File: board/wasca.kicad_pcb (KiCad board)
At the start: 2 copper layers, 0 parts

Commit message: PCB routing started
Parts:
- added C1: 10uF, Capacitors_SMD:C_0603_HandSoldering, F.Cu at (118.5, 90.9)
- added C10: 0.1uF, Capacitors_SMD:C_0603_HandSoldering, F.Cu at (123.1, 117.7)
- added C11: 0.1uF, Capacitors_SMD:C_0603_HandSoldering, F.Cu at (98.6, 121.4)
- added C12: 0.1uF, Capacitors_SMD:C_0603_HandSoldering, F.Cu at (90.4, 114.0)
- added C13: 0.1uF, Capacitors_SMD:C_0603_HandSoldering, F.Cu at (126.5, 109.2)
- added C14: 0.1uF, Capacitors_SMD:C_0603_HandSoldering, F.Cu at (153.3, 128.8)
- added C15: 0.1uF, Capacitors_SMD:C_0603_HandSoldering, F.Cu at (130.6, 123.8)
- added C16: 0.1uF, Capacitors_SMD:C_0603_HandSoldering, F.Cu at (103.0, 113.4)
- added C17: 0.1uF, Capacitors_SMD:C_0603_HandSoldering, F.Cu at (106.3, 126.7)
- added C18: 0.1uF, Capacitors_SMD:C_0603_HandSoldering, F.Cu at (159.4, 99.1)
- added C19: 0.1uF, Capacitors_SMD:C_0603_HandSoldering, F.Cu at (146.6, 96.0)
- added C2: 0.1uF, Capacitors_SMD:C_0603_HandSoldering, F.Cu at (78.1, 116.5)
- added C20: 0.1uF, Capacitors_SMD:C_0603_HandSoldering, F.Cu at (140.8, 113.0)
- added C21: 0.1uF, Capacitors_SMD:C_0603_HandSoldering, F.Cu at (113.9, 121.9)
- added C22: 0.1uF, Capacitors_SMD:C_0603_HandSoldering, F.Cu at (91.6, 126.1)
- added C23: 0.1uF, Capacitors_SMD:C_0603_HandSoldering, F.Cu at (96.1, 114.2)
- added C24: 0.1uF, Capacitors_SMD:C_0603_HandSoldering, F.Cu at (158.9, 117.6)
- added C25: 10uF, Capacitors_SMD:C_1206_HandSoldering, F.Cu at (149.7, 117.6)
- added C26: 0.1uF, Capacitors_SMD:C_0603_HandSoldering, F.Cu at (169.2, 116.2)
- added C27: 0.1uF, Capacitors_SMD:C_0603_HandSoldering, F.Cu at (155.7, 104.6)
- added C28: 0.1uF, Capacitors_SMD:C_0603_HandSoldering, F.Cu at (103.6, 64.6)
- added C29: 0.1uF, Capacitors_SMD:C_0603_HandSoldering, F.Cu at (93.6, 71.6)
- added C3: 0.1uF, Capacitors_SMD:C_0603_HandSoldering, F.Cu at (134.2, 116.0)
- added C30: 0.1uF, Capacitors_SMD:C_0603_HandSoldering, F.Cu at (80.8, 96.3)
- added C31: 0.1uF, Capacitors_SMD:C_0603_HandSoldering, F.Cu at (79.6, 104.9)
- added C32: 0.1uF, Capacitors_SMD:C_0603_HandSoldering, F.Cu at (106.8, 102.2)
- added C33: 10uF, Capacitors_SMD:C_1206_HandSoldering, F.Cu at (116.3, 100.1)
- added C34: 0.1uF, Capacitors_SMD:C_0603_HandSoldering, F.Cu at (125.1, 91.6)
- added C35: 0.1uF, Capacitors_SMD:C_0603_HandSoldering, F.Cu at (140.0, 100.2)
- added C36: 0.1uF, Capacitors_SMD:C_0603_HandSoldering, F.Cu at (83.2, 124.5)
- added C37: 0.1uF, Capacitors_SMD:C_0603_HandSoldering, F.Cu at (112.6, 62.0)
- added C38: 0.1uF, Capacitors_SMD:C_0603_HandSoldering, F.Cu at (97.9, 127.0)
- added C39: 0.1uF, Capacitors_SMD:C_0603_HandSoldering, F.Cu at (140.7, 120.9)
- added C4: 0.1uF, Capacitors_SMD:C_0603_HandSoldering, F.Cu at (106.9, 92.5)
- added C40: 0.1uF, Capacitors_SMD:C_0603_HandSoldering, F.Cu at (88.9, 86.7)
- added C41: 0.1uF, Capacitors_SMD:C_0603_HandSoldering, F.Cu at (89.8, 79.4)
- added C42: 0.1uF, Capacitors_SMD:C_0603_HandSoldering, F.Cu at (128.4, 130.8)
- added C43: 1uF, Capacitors_SMD:C_0603_HandSoldering, F.Cu at (128.1, 100.7)
- added C44: 0.1uF, Capacitors_SMD:C_0603_HandSoldering, F.Cu at (184.4, 61.1)
- added C45: 0.1uF, Capacitors_SMD:C_0603_HandSoldering, F.Cu at (91.6, 63.6)
- added C46: 0.1uF, Capacitors_SMD:C_0603_HandSoldering, F.Cu at (126.0, 53.5)
- added C47: 0.1uF, Capacitors_SMD:C_0603_HandSoldering, F.Cu at (85.1, 73.2)
- added C48: 0.1uF, Capacitors_SMD:C_0603_HandSoldering, F.Cu at (76.1, 89.4)
- added C49: 0.1uF, Capacitors_SMD:C_0603_HandSoldering, F.Cu at (101.0, 59.1)
- added C5: 0.1uF, Capacitors_SMD:C_0603_HandSoldering, F.Cu at (168.0, 130.7)
- added C50: 0.1uF, Capacitors_SMD:C_0603_HandSoldering, F.Cu at (97.5, 89.4)
- added C6: 0.1uF, Capacitors_SMD:C_0603_HandSoldering, F.Cu at (120.3, 125.3)
- added C7: 0.1uF, Capacitors_SMD:C_0603_HandSoldering, F.Cu at (110.0, 118.0)
- added C8: 0.1uF, Capacitors_SMD:C_0603_HandSoldering, F.Cu at (161.8, 109.0)
- added C9: 0.1uF, Capacitors_SMD:C_0603_HandSoldering, F.Cu at (139.8, 127.5)
- added CN1: CARTRIDGE_EDGE_CONNECTOR, Wasca:CARTRIDGE_EDGE_CONNECTOR2, F.Cu at (91.6, 152.3)
- added CON1: SD_Card, Connect:SD_Card_Receptacle, F.Cu at (205.3, 96.1)
- added CON2: USB_OTG, Connect:USB_Micro-B, F.Cu at (76.1, 59.3)
- added D1: D_Schottky_x2_KCom_AAK, Housings_SOT-23_SOT-143_TSOT-6:SOT-23_Handsoldering, F.Cu at (121.2, 61.3)
- added IC1: MT48LC32M16A2TG, Wasca:TSOP_II_54, F.Cu at (133.1, 49.5)
- added L1: L_Small, Resistors_SMD:R_0603_HandSoldering, F.Cu at (83.2, 81.4)
- added R1: 50K, Resistors_SMD:R_0603_HandSoldering, F.Cu at (132.6, 95.6)
- added R2: 50K, Resistors_SMD:R_0603_HandSoldering, F.Cu at (162.4, 58.3)
- added R3: 50K, Resistors_SMD:R_0603_HandSoldering, F.Cu at (147.1, 85.7)
- added R4: 50K, Resistors_SMD:R_0603_HandSoldering, F.Cu at (135.3, 105.5)
- added R5: 50K, Resistors_SMD:R_0603_HandSoldering, F.Cu at (211.3, 75.4)
- added R6: 27, Resistors_SMD:R_0603_HandSoldering, F.Cu at (199.6, 68.8)
- added R7: 27, Resistors_SMD:R_0603_HandSoldering, F.Cu at (191.4, 71.0)
- added R8: 4.7K, Resistors_SMD:R_0603_HandSoldering, F.Cu at (169.8, 109.0)
- added R9: 4.7K, Resistors_SMD:R_0603_HandSoldering, F.Cu at (162.9, 124.0)
- added U1: 74ALVC164245, Housings_SSOP:TSSOP-48_6.1x12.5mm_Pitch0.5mm, F.Cu at (94.5, 100.2)
- added U2: 74ALVC164245, Housings_SSOP:TSSOP-48_6.1x12.5mm_Pitch0.5mm, F.Cu at (134.0, 78.5)
- added U3: 74ALVC164245, Housings_SSOP:TSSOP-48_6.1x12.5mm_Pitch0.5mm, F.Cu at (120.0, 76.9)
- added U4: 74ALVC164245, Housings_SSOP:TSSOP-48_6.1x12.5mm_Pitch0.5mm, F.Cu at (103.6, 78.0)
- added U5: LD1117S33CTR, SMD_Packages:SOT-223, F.Cu at (178.6, 126.4)
- added U6: 10M04SFE144C8G, Housings_QFP:TQFP-144_20x20mm_Pitch0.5mm, F.Cu at (169.4, 82.3)
- added U7: FT201XS, Housings_SSOP:SSOP-16_3.9x4.9mm_Pitch0.635mm, F.Cu at (191.3, 62.7)

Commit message: Route in progress
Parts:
- CN1: footprint Wasca:CARTRIDGE_EDGE_CONNECTOR2 -> libraries:CARTRIDGE_EDGE_CONNECTOR2
- U1: moved to B.Cu
- moved IC1 91.8 mm to (55.0, 97.8), turned to 270 degrees
- moved U6 87.8 mm to (86.5, 111.4), turned to 90 degrees
- moved C8 77.8 mm to (86.7, 129.4)
- moved C5 76.5 mm to (92.3, 141.2)
- moved U3 66.4 mm to (88.3, 135.3), turned to 90 degrees
- moved U4 66.3 mm to (70.1, 135.3), turned to 90 degrees
- moved U2 64.0 mm to (104.4, 135.3), turned to 90 degrees
- moved CN1 52.1 mm to (39.9, 158.3)
- moved C14 43.9 mm to (193.9, 112.3)
- moved C18 43.9 mm to (200.0, 82.5)
- moved C19 43.9 mm to (187.2, 79.5)
- moved C20 43.9 mm to (181.5, 96.5)
- moved C26 43.9 mm to (209.8, 99.7)
- moved C27 43.9 mm to (196.3, 88.1)
- moved C33 43.9 mm to (157.0, 83.6)
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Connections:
- CN1 pad B55: /+5V -> /ABUS_D7
- CN1 pad B56: /+5V -> /ABUS_D6
- CN1 pad B57: /+5V -> /ABUS_D5
- CN1 pad B58: /+5V -> /ABUS_D4
- CN1 pad B60: /+5V -> /ABUS_D15
- CN1 pad B61: /+5V -> /ABUS_D14
- CN1 pad B62: /+5V -> /ABUS_D13
- CN1 pad B63: /+5V -> /ABUS_D12
- U1 pad 11: /ABUS_A10 -> /ABUS_D1
- U1 pad 12: /ABUS_A1 -> /ABUS_D0
- U1 pad 13: /ABUS_D0 -> /ABUS_A1
- U1 pad 14: /ABUS_D1 -> /ABUS_A10
- U1 pad 16: /ABUS_D2 -> /ABUS_A11
- U1 pad 17: /ABUS_D3 -> /ABUS_A9
- U1 pad 19: /ABUS_D8 -> /ABUS_A8
- U1 pad 2: /ABUS_A15 -> /ABUS_D11
- U1 pad 20: /ABUS_D9 -> /ABUS_A13
- U1 pad 22: /ABUS_D10 -> /ABUS_A12
- U1 pad 23: /ABUS_D11 -> /ABUS_A15
- U1 pad 3: /ABUS_A12 -> /ABUS_D10
- U1 pad 5: /ABUS_A13 -> /ABUS_D9
- U1 pad 6: /ABUS_A8 -> /ABUS_D8
- U1 pad 8: /ABUS_A9 -> /ABUS_D3
- U1 pad 9: /ABUS_A11 -> /ABUS_D2
- U2 pad 19: /ABUS_A25 -> /ABUS_A19
- U2 pad 20: /ABUS_A23 -> /ABUS_A21
- U2 pad 22: /ABUS_A21 -> /ABUS_A23
- U2 pad 23: /ABUS_A19 -> /ABUS_A25
- U2 pad 26: /ABUS_3V_A19 -> /ABUS_3V_A25
- U2 pad 27: /ABUS_3V_A21 -> /ABUS_3V_A23
- U2 pad 29: /ABUS_3V_A23 -> /ABUS_3V_A21
- U2 pad 30: /ABUS_3V_A25 -> /ABUS_3V_A19
- U2 pad 31: Net-(U2-Pad31) -> /+3_3V
- U2 pad 42: Net-(U2-Pad42) -> /+3_3V
- U3 pad 13: /+5V -> /ABUS_D12
- U3 pad 14: /+5V -> /ABUS_D13
- U3 pad 16: /+5V -> /ABUS_D14
- U3 pad 17: /+5V -> /ABUS_D15
- U3 pad 19: /+5V -> /ABUS_D4
- U3 pad 20: /+5V -> /ABUS_D5
- U3 pad 22: /+5V -> /ABUS_D6
- U3 pad 23: /+5V -> /ABUS_D7
- U3 pad 26: /ABUS_3V_MUX7 -> /ABUS_3V_MUX0
- U3 pad 27: /ABUS_3V_MUX6 -> /ABUS_3V_MUX1
- U3 pad 29: /ABUS_3V_MUX5 -> /ABUS_3V_MUX2
- U3 pad 30: /ABUS_3V_MUX4 -> /ABUS_3V_MUX3
- U3 pad 32: /ABUS_3V_MUX3 -> /ABUS_3V_MUX4
- U3 pad 33: /ABUS_3V_MUX2 -> /ABUS_3V_MUX5
- U3 pad 35: /ABUS_3V_MUX1 -> /ABUS_3V_MUX6
- U3 pad 36: /ABUS_3V_MUX0 -> /ABUS_3V_MUX7
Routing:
- net /ABUS_A25: track 0.00 -> 54.9 mm, vias 0 -> 1
- net GND: track 0.00 -> 54.5 mm, vias 0 -> 5
- net /ABUS_A23: track 0.00 -> 52.9 mm, vias 0 -> 1
- net /ABUS_A21: track 0.00 -> 48.7 mm, vias 0 -> 1
- net /ABUS_D12: track 0.00 -> 47.3 mm, vias 0 -> 2
- net /ABUS_A19: track 0.00 -> 46.6 mm, vias 0 -> 1
- net /ABUS_D13: track 0.00 -> 44.5 mm, vias 0 -> 2
- net /ABUS_D14: track 0.00 -> 41.1 mm, vias 0 -> 2
- net /ABUS_D15: track 0.00 -> 38.5 mm, vias 0 -> 2
- net /ABUS_D4: track 0.00 -> 38.0 mm, vias 0 -> 2
- net /ABUS_D5: track 0.00 -> 34.6 mm, vias 0 -> 2
- net /ABUS_D6: track 0.00 -> 31.8 mm, vias 0 -> 2
- net /ABUS_D7: track 0.00 -> 29.4 mm, vias 0 -> 2
- net /+5V: track 0.00 -> 29.4 mm, vias 0 -> 2
- net /ABUS_WR1: track 0.00 -> 22.0 mm
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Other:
- net class Default: clearance 0.2 -> 0.2032; trace_width 0.25 -> 0.2032; via_dia 0.6 -> 0.889; via_drill 0.4 -> 0.381
- rule pad_to_mask_clearance: 0 -> 0.254
- rule trace_clearance: 0.2 -> 0.2032
- rule trace_min: 0.2 -> 0.2032
- rule via_min_drill: 0.3 -> 0.381
- rule via_min_size: 0.4 -> 0.889

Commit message: Half-routed
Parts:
- U2: moved to B.Cu
- moved C5 29.7 mm to (119.0, 128.2)
- moved U6 23.2 mm to (63.6, 107.4)
- moved C6 21.0 mm to (122.4, 125.7)
- moved C9 19.6 mm to (122.6, 130.9)
- moved IC1 18.5 mm to (36.8, 101.2)
- moved U1 14.8 mm to (96.5, 120.7)
- moved U2 6.27 mm to (98.5, 137.5)
- moved U3 1.32 mm to (86.9, 135.2)
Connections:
- U2 pad 11: /ABUS_CS2 -> /ABUS_CS0
- U2 pad 12: /ABUS_WR0 -> /ABUS_TIM1
- U2 pad 13: /ABUS_FC0 -> /ABUS_FC1
- U2 pad 14: /ABUS_TIM0 -> /ABUS_WR1
- U2 pad 16: /ABUS_TIM2 -> /ABUS_CS1
- U2 pad 17: /ABUS_AS -> /ABUS_RD
- U2 pad 19: /ABUS_A19 -> /ABUS_A25
- U2 pad 2: /ABUS_RD -> /ABUS_AS
- U2 pad 20: /ABUS_A21 -> /ABUS_A23
- U2 pad 22: /ABUS_A23 -> /ABUS_A21
- U2 pad 23: /ABUS_A25 -> /ABUS_A19
- U2 pad 3: /ABUS_CS1 -> /ABUS_TIM2
- U2 pad 5: /ABUS_WR1 -> /ABUS_TIM0
- U2 pad 6: /ABUS_FC1 -> /ABUS_FC0
- U2 pad 8: /ABUS_TIM1 -> /ABUS_WR0
- U2 pad 9: /ABUS_CS0 -> /ABUS_CS2
- U3 pad 13: /ABUS_D12 -> /ABUS_D7
- U3 pad 14: /ABUS_D13 -> /ABUS_D6
- U3 pad 16: /ABUS_D14 -> /ABUS_D5
- U3 pad 17: /ABUS_D15 -> /ABUS_D4
- U3 pad 19: /ABUS_D4 -> /ABUS_D15
- U3 pad 20: /ABUS_D5 -> /ABUS_D14
- U3 pad 22: /ABUS_D6 -> /ABUS_D13
- U3 pad 23: /ABUS_D7 -> /ABUS_D12
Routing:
- net GND: track 54.5 -> 200.3 mm, vias 5 -> 12
- net /+5V: track 29.4 -> 143.0 mm, vias 2 -> 11
- net /ABUS_WAIT: track 0.00 -> 75.3 mm, vias 0 -> 2
- net /ABUS_3V_RD: track 0.00 -> 66.9 mm, vias 0 -> 3
- net /ABUS_IRQ: track 0.00 -> 65.0 mm, vias 0 -> 2
- net /ABUS_3V_FC1: track 0.00 -> 64.6 mm, vias 0 -> 3
- net /ABUS_3V_WR1: track 0.00 -> 62.9 mm, vias 0 -> 3
- net /ABUS_3V_TIM1: track 0.00 -> 62.3 mm, vias 0 -> 3
- net /ABUS_3V_CS1: track 0.00 -> 62.1 mm, vias 0 -> 3
- net /RESET: track 0.00 -> 36.9 mm, vias 0 -> 1
- net /ABUS_3V_MUX_DATA_DIR: track 0.00 -> 23.6 mm, vias 0 -> 3
- net /ABUS_D0: track 15.8 -> 37.3 mm
- net /ABUS_D1: track 16.0 -> 37.0 mm
- net /ABUS_D12: track 47.3 -> 26.7 mm, vias 2 -> 0
- net /ABUS_D2: track 16.0 -> 36.4 mm
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
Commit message: Routed at last.
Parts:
- removed C17, C18, C19, C20, C21, C22, C29, C30, C49: 0.1uF, Capacitors_SMD:C_0603_HandSoldering
- added CON3: Thermal_Quad, Wasca:Termal_Quad, F.Cu at (63.6, 107.4)
- C10, C11, C12, C14, C15, C16, C23, C24, C26, C28, C3, C31, C32, C33, C34, C35, C36, C37, C38, C39, C41, C42, C43, C47, C5, C50, C7, C8, CON1, L1, R1, R5: moved to B.Cu
- D1: value D_Schottky_x2_KCom_AAK -> D_Schottky_x2_KCom
- moved R5 208.2 mm to (59.7, 138.8)
- moved CON1 201.1 mm to (52.8, 135.6)
- moved R2 185.2 mm to (42.2, 133.6)
- moved R3 147.7 mm to (54.5, 133.0)
- moved C24 144.4 mm to (55.1, 100.2)
- moved C39 144.2 mm to (37.2, 107.7), turned to 90 degrees
- moved R1 143.4 mm to (43.0, 139.2), turned to 90 degrees
- moved C3 141.7 mm to (40.5, 144.2), turned to 180 degrees
- moved C26 136.2 mm to (73.6, 98.7), turned to 180 degrees
- moved C43 135.3 mm to (45.3, 139.4), turned to 90 degrees
- moved U7 131.0 mm to (110.8, 96.1), turned to 90 degrees
- moved R6 130.7 mm to (117.3, 96.7), turned to 180 degrees
- moved R4 126.9 mm to (57.7, 135.1)
- moved C35 125.8 mm to (56.5, 104.7)
- moved C42 125.5 mm to (44.2, 100.8), turned to 90 degrees
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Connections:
- CON1 pad 12: Net-(CON1-Pad12) -> GND
- CON1 pad 13: Net-(CON1-Pad12) -> GND
- D1 pad 2: /+5V -> Net-(C25-Pad1)
- D1 pad 3: Net-(D1-Pad3) -> /+5V
- IC1 pad 36: /SDR_A11 -> /SDR_A12
- U2 pad 26: /ABUS_3V_A25 -> /ABUS_3V_A19
- U2 pad 27: /ABUS_3V_A23 -> /ABUS_3V_A21
- U2 pad 29: /ABUS_3V_A21 -> /ABUS_3V_A23
- U2 pad 30: /ABUS_3V_A19 -> /ABUS_3V_A25
- U2 pad 32: /ABUS_3V_AS -> /ABUS_3V_RD
- U2 pad 33: /ABUS_3V_TIM2 -> /ABUS_3V_CS1
- U2 pad 35: /ABUS_3V_TIM0 -> /ABUS_3V_WR1
- U2 pad 36: /ABUS_3V_FC0 -> /ABUS_3V_FC1
- U2 pad 37: /ABUS_3V_WR0 -> /ABUS_3V_TIM1
- U2 pad 38: /ABUS_3V_CS2 -> /ABUS_3V_CS0
- U2 pad 40: /ABUS_3V_CS0 -> /ABUS_3V_CS2
- U2 pad 41: /ABUS_3V_TIM1 -> /ABUS_3V_WR0
- U2 pad 43: /ABUS_3V_FC1 -> /ABUS_3V_FC0
- U2 pad 44: /ABUS_3V_WR1 -> /ABUS_3V_TIM0
- U2 pad 46: /ABUS_3V_CS1 -> /ABUS_3V_TIM2
- U2 pad 47: /ABUS_3V_RD -> /ABUS_3V_AS
- U6 pad 10: /ABUS_3V_A20 -> Net-(CON1-Pad1)
- U6 pad 100: /SDR_A11 -> /SDR_DQ6
- U6 pad 101: /SDR_A10 -> /SDR_DQ5
- U6 pad 102: /SDR_A9 -> /SDR_DQ0
- U6 pad 105: /SDR_A8 -> /SDR_DQ1
- U6 pad 106: /SDR_A7 -> /SDR_DQ2
- U6 pad 11: /ABUS_3V_A18 -> /ABUS_3V_A17
- U6 pad 110: /SDR_A6 -> /SDR_DQ3
- U6 pad 111: /SDR_A5 -> /SDR_DQ4
- U6 pad 112: /SDR_A4 -> /SDR_DQ15
- U6 pad 113: /SDR_A3 -> /SDR_DQ14
- U6 pad 114: /SDR_A2 -> /SDR_DQ13
- U6 pad 118: /SDR_A1 -> /SDR_DQ12
- U6 pad 119: /SDR_A0 -> /SDR_DQ11
- U6 pad 12: /ABUS_3V_MUX_EN1 -> /ABUS_3V_A24
- U6 pad 120: /SDR_DQMH -> /SDR_DQ10
- U6 pad 121: /SDR_DQML -> /SDR_DQ9
- U6 pad 123: /SDR_DQ15 -> /SDR_DQ8
- U6 pad 124: /SDR_DQ14 -> /SDR_DQMH
- U6 pad 127: Net-(U6-Pad127) -> /SDR_CLK
- U6 pad 13: /ABUS_3V_MUX_EN2 -> /ABUS_3V_A22
- U6 pad 130: Net-(U6-Pad130) -> /SDR_CKE
- U6 pad 131: Net-(U6-Pad131) -> /SDR_A12
- U6 pad 132: Net-(U6-Pad132) -> /SDR_A11
- U6 pad 134: Net-(U6-Pad134) -> /SDR_A9
- U6 pad 135: Net-(U6-Pad135) -> /SDR_A8
- U6 pad 136: Net-(CON1-Pad7) -> /SDR_A7
- U6 pad 138: Net-(CON1-Pad5) -> /SDR_A6
- U6 pad 139: Net-(U6-Pad139) -> /+3_3V
- U6 pad 14: /ABUS_3V_MUX_DATA_DIR -> /ABUS_3V_A20
- U6 pad 140: Net-(CON1-Pad2) -> /SDR_A5
- U6 pad 141: Net-(CON1-Pad1) -> /SDR_A4
- U6 pad 17: /ABUS_3V_A16 -> /ABUS_3V_A18
- U6 pad 21: /ABUS_3V_FC1 -> /ABUS_3V_A16
- U6 pad 22: /ABUS_3V_TIM1 -> /RESET_3V
- U6 pad 24: /ABUS_3V_CS0 -> /DOTCLK_3V
- U6 pad 25: /ABUS_3V_CS2 -> /ABUS_3V_WAIT
- U6 pad 26: /DOTCLK_3V -> /ABUS_3V_IRQ
- U6 pad 27: /ABUS_3V_RD -> /ABUS_3V_MUX_EN1
- U6 pad 28: /ABUS_3V_WR0 -> /ABUS_3V_MUX0
- U6 pad 29: /ABUS_3V_WR1 -> /ABUS_3V_MUX1
- U6 pad 30: /RESET_3V -> /ABUS_3V_MUX2
- U6 pad 32: /ABUS_3V_CS1 -> /ABUS_3V_MUX3
- U6 pad 33: /ABUS_3V_FC0 -> /ABUS_3V_MUX4
- U6 pad 38: /ABUS_3V_TIM0 -> /ABUS_3V_MUX5
- U6 pad 39: /ABUS_3V_TIM2 -> /ABUS_3V_MUX6
- U6 pad 41: /ABUS_3V_AS -> /ABUS_3V_MUX7
- U6 pad 43: /ABUS_3V_A25 -> /ABUS_3V_MUX_EN2
- U6 pad 44: /ABUS_3V_A23 -> /ABUS_3V_MUX_DATA_DIR
- U6 pad 45: /ABUS_3V_A21 -> /ABUS_3V_A19
- U6 pad 46: /ABUS_3V_A19 -> /ABUS_3V_A21
- U6 pad 47: /ABUS_3V_WAIT -> /ABUS_3V_A23
- U6 pad 48: /ABUS_3V_IRQ -> /ABUS_3V_A25
- U6 pad 50: /ABUS_3V_MUX0 -> /ABUS_3V_RD
- U6 pad 52: /ABUS_3V_MUX1 -> /ABUS_3V_CS1
- U6 pad 54: /ABUS_3V_MUX2 -> /ABUS_3V_WR1
- U6 pad 55: /ABUS_3V_MUX3 -> /ABUS_3V_FC1
- U6 pad 56: /ABUS_3V_MUX4 -> /ABUS_3V_TIM1
- U6 pad 57: /ABUS_3V_MUX5 -> /ABUS_3V_CS0
- U6 pad 58: /ABUS_3V_MUX6 -> /ABUS_3V_CS2
- U6 pad 59: /ABUS_3V_MUX7 -> /ABUS_3V_WR0
- U6 pad 6: /ABUS_3V_A17 -> Net-(CON1-Pad7)
- U6 pad 60: /ABUS_3V_MUX8 -> /ABUS_3V_FC0
- U6 pad 61: /ABUS_3V_MUX9 -> /ABUS_3V_TIM0
- U6 pad 62: /ABUS_3V_MUX10 -> /ABUS_3V_TIM2
- U6 pad 64: /ABUS_3V_MUX11 -> /ABUS_3V_AS
- U6 pad 65: /ABUS_3V_MUX12 -> /ABUS_3V_MUX15
- U6 pad 66: /ABUS_3V_MUX13 -> /ABUS_3V_MUX14
- U6 pad 69: /ABUS_3V_MUX14 -> /ABUS_3V_MUX13
- U6 pad 7: /ABUS_3V_A24 -> Net-(CON1-Pad5)
- U6 pad 70: /ABUS_3V_MUX15 -> /ABUS_3V_MUX12
- U6 pad 74: /SDR_DQ13 -> /ABUS_3V_MUX11
- U6 pad 75: /SDR_DQ12 -> /ABUS_3V_MUX10
- U6 pad 76: /SDR_DQ11 -> /ABUS_3V_MUX9
- U6 pad 77: /SDR_DQ10 -> /ABUS_3V_MUX8
- U6 pad 78: /SDR_DQ9 -> /USB_SCL
- U6 pad 79: /SDR_DQ8 -> /USB_SDA
- U6 pad 8: /ABUS_3V_A22 -> Net-(CON1-Pad2)
- U6 pad 80: /SDR_DQ7 -> /USB_CBUS1
- U6 pad 81: /SDR_DQ6 -> /USB_CBUS0
- U6 pad 84: /SDR_DQ5 -> Net-(U6-Pad84)
- U6 pad 85: /SDR_DQ4 -> /SDR_A3
- U6 pad 86: /SDR_DQ3 -> /SDR_A2
- U6 pad 87: /SDR_DQ2 -> /SDR_A1
- U6 pad 88: /SDR_DQ1 -> /SDR_A0
- U6 pad 89: /SDR_DQ0 -> /SDR_A10
- U6 pad 90: /SDR_CS -> /SDR_BA1
- U6 pad 91: /SDR_WE -> /SDR_BA0
- U6 pad 92: /SDR_CAS -> /SDR_CS
- U6 pad 96: /SDR_CKE -> /SDR_CAS
- U6 pad 97: /SDR_CLK -> /SDR_WE
- U6 pad 98: /SDR_BA1 -> /SDR_DQML
- U6 pad 99: /SDR_BA0 -> /SDR_DQ7
- U7 pad 14: Net-(U6-Pad130) -> /USB_CBUS1
- U7 pad 15: Net-(U6-Pad131) -> /USB_CBUS0
- U7 pad 2: Net-(U6-Pad134) -> /USB_SCL
- U7 pad 4: Net-(U6-Pad132) -> /USB_SDA
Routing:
- net GND: track 200.3 -> 972.5 mm, vias 12 -> 53
- net /+3_3V: track 0.00 -> 485.3 mm, vias 0 -> 29
- net /+5V: track 143.0 -> 294.8 mm, vias 11 -> 17
- net Net-(C23-Pad1): track 0.00 -> 93.0 mm, vias 0 -> 4
- net /SDR_A3: track 0.00 -> 70.8 mm
- net /SDR_A2: track 0.00 -> 68.4 mm
- net /SDR_A1: track 0.00 -> 65.8 mm
- net /SDR_A0: track 0.00 -> 63.2 mm
- net /SDR_A10: track 0.00 -> 60.6 mm
- net /ABUS_3V_MUX_EN1: track 0.00 -> 59.0 mm, vias 0 -> 3
- net /SDR_BA1: track 0.00 -> 57.8 mm
- net /SDR_BA0: track 0.00 -> 55.5 mm
- net /ABUS_3V_MUX8: track 0.00 -> 55.4 mm, vias 0 -> 2
- net /ABUS_3V_MUX9: track 0.00 -> 53.1 mm, vias 0 -> 2
- net /SDR_CS: track 0.00 -> 53.1 mm
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- added copper zone on B.Cu, net GND
- added copper zone on F.Cu, net GND

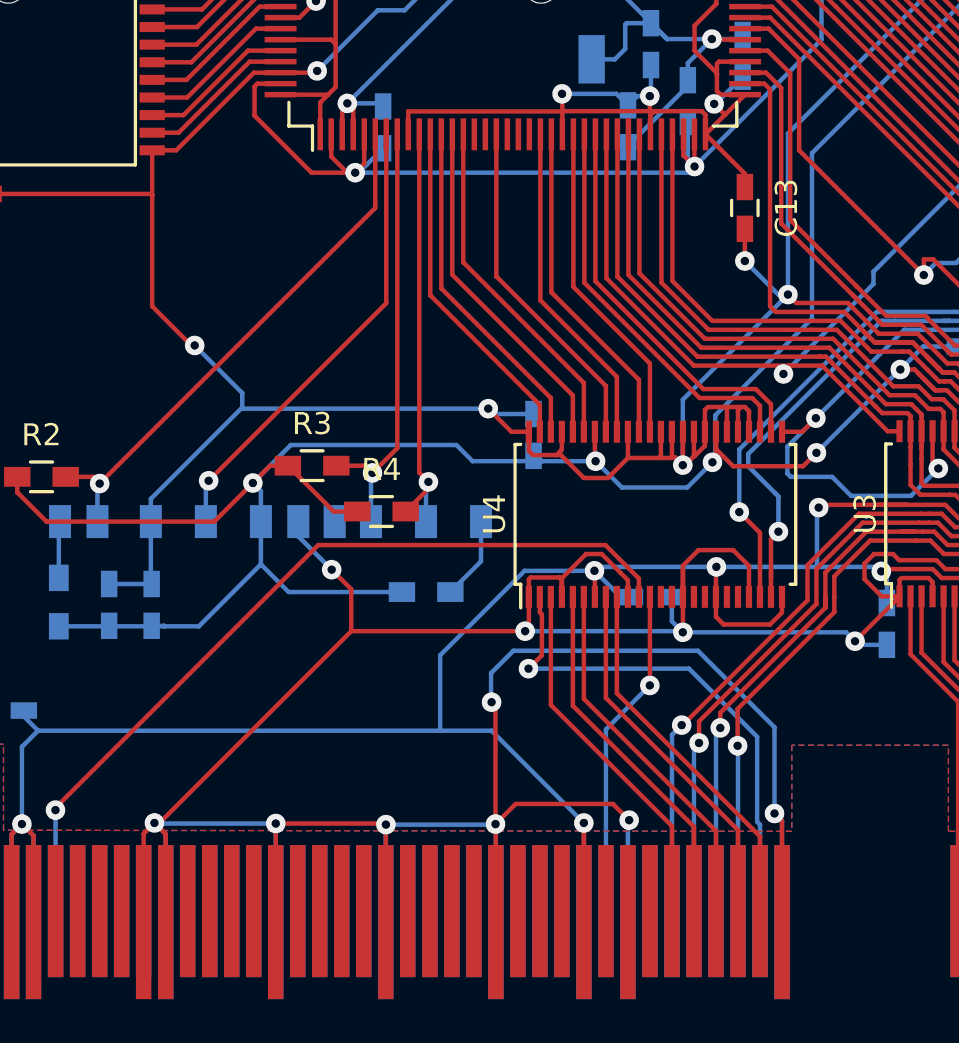
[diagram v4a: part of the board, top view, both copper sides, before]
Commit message: SCSP 22.57 MHz clock is used instead of 27..29 MHz MCLK2
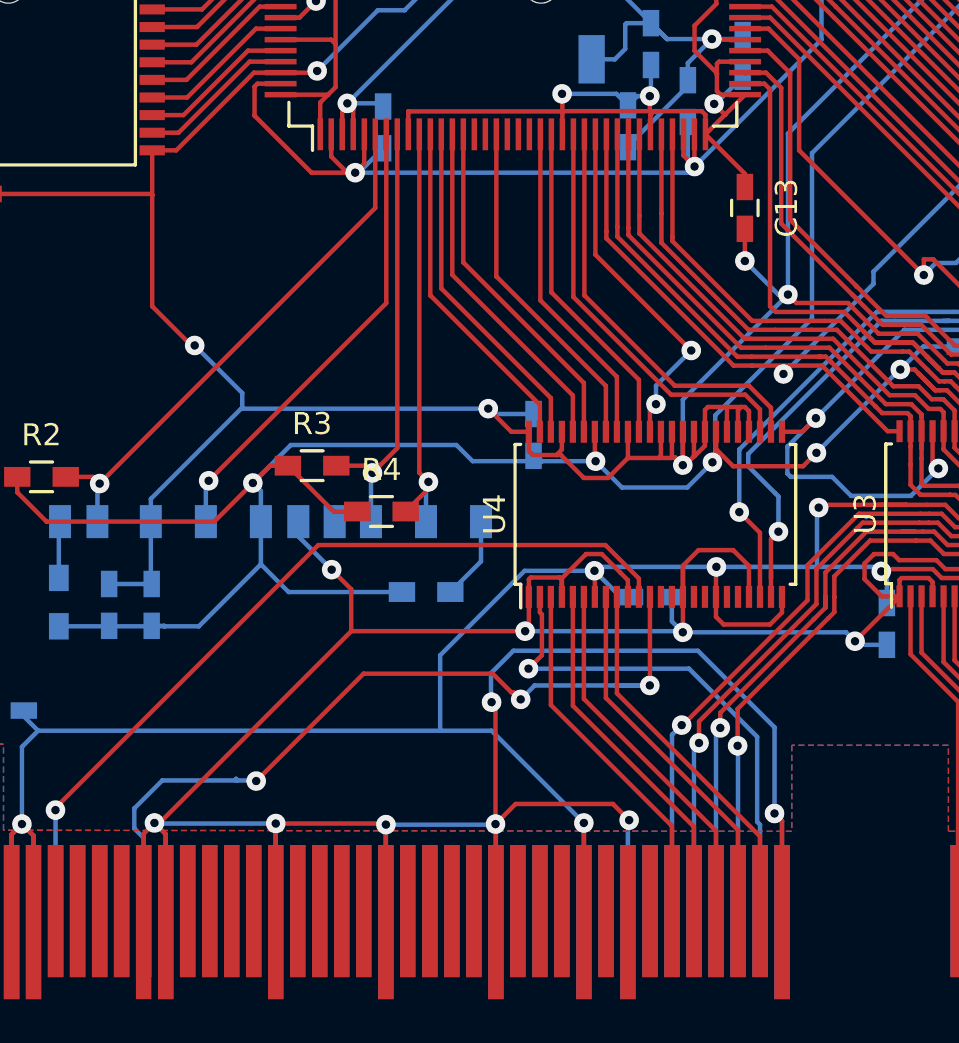
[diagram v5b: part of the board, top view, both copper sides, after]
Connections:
- CN1 pad A28: /DOTCLK -> Net-(CN1-PadA28)
- CN1 pad A7: Net-(CN1-PadA7) -> /SCSPCLK
- U4 pad 12: /DOTCLK -> /SCSPCLK
- U4 pad 37: /DOTCLK_3V -> /SCSPCLK_3V
- U6 pad 24: /DOTCLK_3V -> /ABUS_3V_WAIT
- U6 pad 25: /ABUS_3V_WAIT -> /ABUS_3V_IRQ
- U6 pad 26: /ABUS_3V_IRQ -> /SCSPCLK_3V
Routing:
- net /SCSPCLK: track 0.00 -> 37.3 mm, vias 0 -> 3
- net /SCSPCLK_3V: track 0.00 -> 16.1 mm, vias 0 -> 2
- net /DOTCLK: track 15.1 -> 0.00 mm, vias 1 -> 0
- net /DOTCLK_3V: track 15.0 -> 0.00 mm
- net /ABUS_3V_MUX0: track 38.3 -> 37.3 mm
- net /ABUS_3V_MUX1: track 37.0 -> 35.9 mm
- net /ABUS_3V_MUX3: track 32.5 -> 31.4 mm
- net /ABUS_3V_MUX_EN1: track 59.0 -> 57.9 mm
- net /ABUS_3V_MUX2: track 34.1 -> 33.0 mm
- net /ABUS_3V_MUX4: track 30.8 -> 29.7 mm
- net /ABUS_3V_IRQ: track 18.2 -> 19.0 mm
- net /ABUS_3V_WAIT: track 18.2 -> 19.0 mm
